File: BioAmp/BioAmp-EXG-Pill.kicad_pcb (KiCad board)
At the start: 4 copper layers, 39.2 x 11 mm, 44 parts, among them IC1 MCP3221A4T-E_OT, IC3 MAX1169BEUD+, J2 Conn_01x04_Pin, J3 Conn_01x04_Pin, J4 522710469, U1 TL074HIPWR

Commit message: Did component placement
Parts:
- removed IC1: MCP3221A4T-E_OT, ADC:SOT95P280X145-5N
- removed the R11 at (121.6, 98.2)
- C10, C11, C9: footprint Capacitor_SMD:C_0603_1608Metric_Pad1.08x0.95mm_HandSolder -> Capacitor_SMD:C_0402_1005Metric
- C4, D1, D2, D3, D4, D5, D6, JP4, JP5, JP6, R12, R13, R14, R17, R18, R19, R6: moved to B.Cu
- J4: footprint fpc_con:CON_522710469_MOL -> FPC_Connector:CON_522710469_MOL
- moved D1 77.9 mm to (115.8, 90.0)
- moved D2 77.7 mm to (115.8, 93.7)
- moved D3 75.5 mm to (118.0, 97.4)
- moved JP6 61.8 mm to (129.3, 91.2), turned to 90 degrees
- moved JP5 58.8 mm to (131.7, 91.2), turned to 90 degrees
- moved D4 58.2 mm to (136.6, 88.8)
- moved D6 57.6 mm to (137.1, 92.9), turned to 90 degrees
- moved R17 57.6 mm to (128.9, 93.5), turned to 180 degrees
- moved R14 57.3 mm to (114.6, 92.6), turned to 180 degrees
- moved R13 57.1 mm to (114.6, 91.2), turned to 180 degrees
- moved D5 56.9 mm to (137.1, 95.2), turned to -90 degrees
- moved JP4 55.9 mm to (134.2, 91.2), turned to 90 degrees
- moved R11 55.4 mm to (115.4, 98.7)
- moved R18 54.1 mm to (132.2, 93.5)
- moved R12 53.2 mm to (117.9, 92.6), turned to 180 degrees
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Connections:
- net Net-(R5-Pad1) renamed /U1A_out
- net Net-(U1B--) renamed /U1B_in
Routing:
- net VCC: track 52.1 -> 24.5 mm, vias 4 -> 2
- net bpfIN: track 26.7 -> 0.00 mm, vias 2 -> 0
- net /IN+_Prot: track 23.4 -> 0.00 mm
- net /IN-_Prot: track 21.8 -> 0.00 mm
- net bpfOUT: track 20.6 -> 0.00 mm, vias 2 -> 0
- net ampRef: track 12.7 -> 0.00 mm
- net /U1B_in: track 10.6 -> 0.00 mm, vias 2 -> 0
- net DRL: track 10.1 -> 0.00 mm
- net Net-(U1D-+): track 7.98 -> 0.00 mm
- net Net-(U1A--): track 7.16 -> 0.00 mm
- net inaOUT: track 8.46 -> 2.13 mm
- net SCL: track 12.1 -> 7.45 mm, vias 0 -> 1
- net /U1A_out: track 3.68 -> 0.00 mm
- net Net-(C1-Pad2): track 1.88 -> 0.00 mm
- net GND: track 1.51 -> 0.00 mm, vias 3 -> 1
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- added copper zone on In1.Cu, net GND
- added copper zone on In2.Cu, net GND
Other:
- board size 39.2 x 11 mm -> 43.2 x 13.1 mm

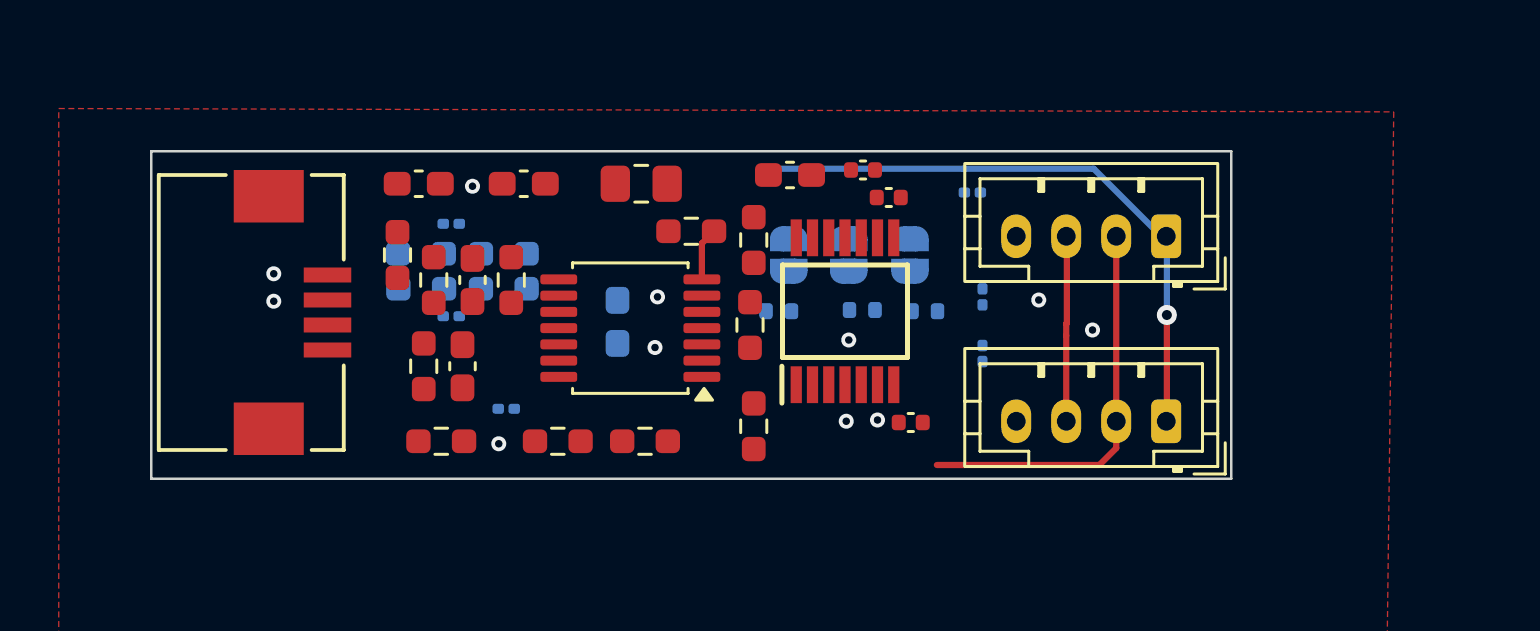
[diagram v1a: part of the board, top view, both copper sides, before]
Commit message: Added rounded edge with mounting hole
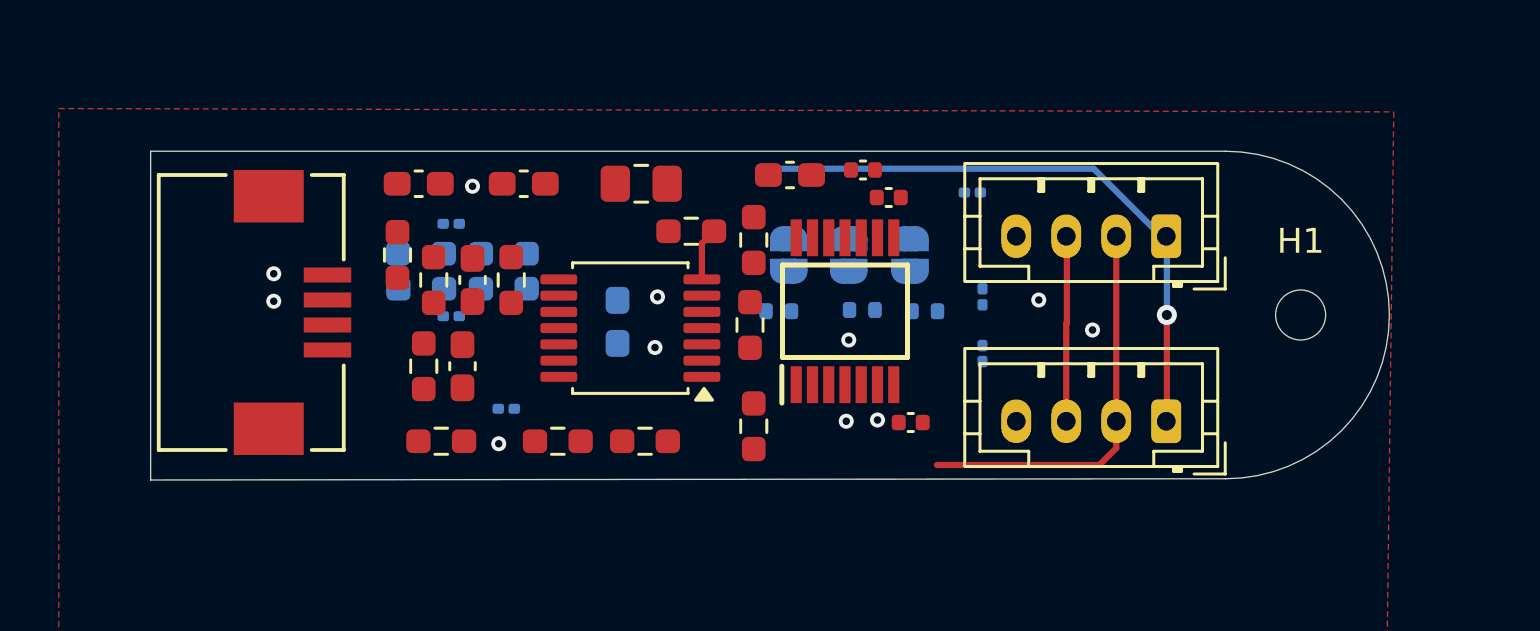
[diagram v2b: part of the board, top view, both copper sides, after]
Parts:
- added H1: MountingHole_Pad, MountingHole:MountingHole_2mm, F.Cu at (149.8, 93.7)
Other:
- board size 43.2 x 13.1 mm -> 49.5 x 13.2 mm
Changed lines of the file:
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@@
 		)
 		(embedded_fonts no)
+		(model "${CON_522710469_MOL}/2026-09-26_13-00-23.kicad_sym"
+			(offset
+				(xyz 0 0 0)
+			)
+			(scale
+				(xyz 1 1 1)
+			)
+			(rotate
+				(xyz 0 0 0)
+			)
+		)
 	)
 	(footprint "Capacitor_SMD:C_0805_2012Metric_Pad1.18x1.45mm_HandSolder"
@@
 		)
 	)
+	(footprint "MountingHole:MountingHole_2mm"
+		(layer "F.Cu")
+		(at 149.775 93.65)
+		(descr "Mounting Hole 2mm, no annular, generated by kicad-footprint-generator mountinghole.py")
+		(tags "mountinghole")
+		(property "Reference" "H1"
+			(at 0 -2.95 0)
+			(layer "F.SilkS")
+			(effects
+				(font
+					(size 1 1)
+					(thickness 0.15)
+				)
+			)
+		)
+		(property "Value" "MountingHole_Pad"
+			(at 0 2.95 0)
+			(layer "F.Fab")
+			(effects
+				(font
+					(size 1 1)
+					(thickness 0.15)
+				)
+			)
+		)
+		(property "Datasheet" ""
+			(at 0 0 0)
+			(layer "F.Fab")
+			(hide yes)
+			(effects
+				(font
+					(size 1.27 1.27)
+				)
+			)
+		)
+		(property "Description" "Mounting Hole with connection"
+			(at 0 0 0)
+			(layer "F.Fab")
+			(hide yes)
+			(effects
+				(font
+					(size 1.27 1.27)
+				)
+			)
+		)
+		(property "KiLib_Generator" "mounting_hardware/mounting_hole"
+			(at 0 0 0)
+			(layer "F.SilkS")
+			(hide yes)
+			(effects
+				(font
+					(size 1 1)
+					(thickness 0.15)
+				)
+			)
+		)
+		(property ki_fp_filters "MountingHole*Pad*")
+		(sheetname "/")
+		(sheetfile "BioAmp-EXG-Pill.kicad_sch")
+		(units
+			(unit
+				(name "A")
+				(pins "1")
+			)
+		)
+		(attr exclude_from_bom)
+		(duplicate_pad_numbers_are_jumpers no)
+		(fp_circle
+			(center 0 0)
+			(end 2 0)
+			(stroke
+				(width 0.15)
+				(type solid)
+			)
+			(fill no)
+			(layer "Cmts.User")
+		)
+		(fp_circle
+			(center 0 0)
+			(end 2.25 0)
+			(stroke
+				(width 0.05)
+				(type solid)
+			)
+			(fill no)
+			(layer "F.CrtYd")
+		)
+		(fp_text user "${REFERENCE}"
+			(at 0 0 0)
+			(layer "F.Fab")
+			(effects
+				(font
+					(size 1 1)
+					(thickness 0.15)
+				)
+			)
+		)
+		(pad "" np_thru_hole circle
+			(at 0 0)
+			(size 2 2)
+			(drill 2)
+			(layers "*.Cu" "*.Mask")
+		)
+		(embedded_fonts no)
+	)
 	(footprint "Resistor_SMD:R_0603_1608Metric_Pad0.98x0.95mm_HandSolder"
 		(layer "F.Cu")
@@
 	)
 	(gr_line
-		(start 148.3 100.15)
-		(end 147.3 100.15)
+		(start 153.4 93.65)
+		(end 153.375 109.475)
 		(stroke
 			(width 0.1)
@@
 	)
 	(gr_line
-		(start 148.9 87.05)
-		(end 147.25 87.05)
+		(start 103.775 87.1)
+		(end 103.775 100.25)
 		(stroke
-			(width 0.1)
+			(width 0.05)
 			(type default)
 		)
-		(layer "Dwgs.User")
+		(layer "Edge.Cuts")
 	)
-	(gr_rect
-		(start 103.8 87.1)
-		(end 147 100.2)
+	(gr_line
+		(start 103.775 100.25)
+		(end 146.775 100.2)
 		(stroke
-			(width 0.1)
-			(type solid)
+			(width 0.05)
+			(type default)
+		)
+		(layer "Edge.Cuts")
+	)
+	(gr_line
+		(start 146.775 87.1)
+		(end 103.775 87.1)
+		(stroke
+			(width 0.05)
+			(type default)
+		)
+		(layer "Edge.Cuts")
+	)
+	(gr_arc
+		(start 146.775 87.1)
+		(mid 153.325 93.65)
+		(end 146.775 100.2)
+		(stroke
+			(width 0.05)
+			(type default)
 		)
-		(fill no)
 		(layer "Edge.Cuts")
 	)
@@
 		(layer "Dwgs.User")
 		(pts
-			(xy 103.85 107.75) (xy 147 100.6)
+			(xy 103.85 107.75) (xy 153.35 107.75)
 		)
 		(height 0)
@@
 			(keep_text_aligned yes)
 		)
-		(gr_text "43.1500 mm"
-			(at 125.425 106.6 0)
+		(gr_text "49.5000 mm"
+			(at 128.6 106.6 0)
 			(layer "Dwgs.User")
 			(effects
@@
 		(layer "Dwgs.User")
 		(pts
-			(xy 148.9 87.05) (xy 149.3 100.15)
+			(xy 161.675 87.05) (xy 162.075 100.15)
 		)
 		(height 0)
@@
 		)
 		(gr_text "13.1000 mm"
-			(at 147.75 93.6 90)
+			(at 160.525 93.6 90)
 			(layer "Dwgs.User")
 			(effects
@@
 		)
 	)
+	(dimension
+		(type orthogonal)
+		(layer "Edge.Cuts")
+		(pts
+			(xy 146.775 93.65) (xy 153.325 93.65)
+		)
+		(height 0)
+		(orientation 0)
+		(format
+			(prefix "")
+			(suffix "")
+			(units 3)
+			(units_format 1)
+			(precision 4)
+		)
+		(style
+			(thickness 0.05)
+			(arrow_length 1.27)
+			(text_position_mode 0)
+			(arrow_direction outward)
+			(extension_height 0.58642)
+			(extension_offset 0.5)
+			(keep_text_aligned yes)
+		)
+		(gr_text "6.5500 mm"
+			(at 150.05 92.5 0)
+			(layer "Edge.Cuts")
+			(effects
+				(font
+					(size 1 1)
+					(thickness 0.15)
+				)
+			)
+		)
+	)
 	(segment
 		(start 144.425 97.9)
@@
 	)
 	(via
-		(at 141.45 94.25)
+		(at 108.7 92)
 		(size 0.6)
 		(drill 0.3)
 		(layers "F.Cu" "B.Cu")
 		(free yes)
-		(net "GND")
+		(net "IN-")
+	)
+	(via
+		(at 108.7 93.1)
+		(size 0.6)
+		(drill 0.3)
+		(layers "F.Cu" "B.Cu")
+		(free yes)
+		(net "IN+")
 	)
 	(segment
@@
 		(net "SDA")
 	)
-	(via
-		(at 108.7 92)
-		(size 0.6)
-		(drill 0.3)
-		(layers "F.Cu" "B.Cu")
-		(free yes)
-		(net "IN-")
-	)
-	(via
-		(at 108.7 93.1)
-		(size 0.6)
-		(drill 0.3)
-		(layers "F.Cu" "B.Cu")
-		(free yes)
-		(net "IN+")
-	)
-	(via
-		(at 124.05 92.925)
-		(size 0.6)
-		(drill 0.3)
-		(layers "F.Cu" "B.Cu")
-		(free yes)
-		(net "/IN+_Prot")
-	)
-	(via
-		(at 123.95 94.95)
-		(size 0.6)
-		(drill 0.3)
-		(layers "F.Cu" "B.Cu")
-		(free yes)
-		(net "/IN-_Prot")
-	)
 	(segment
 		(start 140.4 94.475)
@@
 		(net "SCL")
 	)
+	(via
+		(at 141.45 94.25)
+		(size 0.6)
+		(drill 0.3)
+		(layers "F.Cu" "B.Cu")
+		(free yes)
+		(net "GND")
+	)
+	(via
+		(at 123.95 94.95)
+		(size 0.6)
+		(drill 0.3)
+		(layers "F.Cu" "B.Cu")
+		(free yes)
+		(net "/IN-_Prot")
+	)
+	(via
+		(at 124.05 92.925)
+		(size 0.6)
+		(drill 0.3)
+		(layers "F.Cu" "B.Cu")
+		(free yes)
+		(net "/IN+_Prot")
+	)
 	(segment

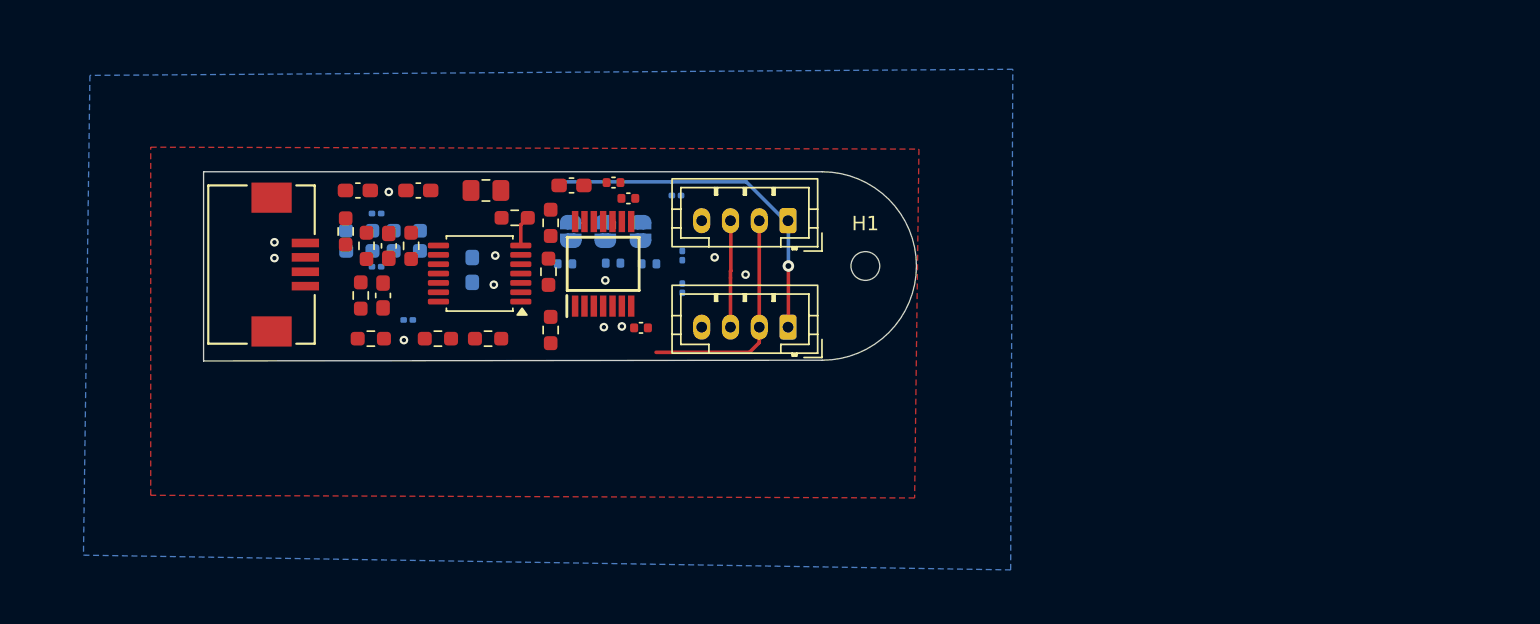
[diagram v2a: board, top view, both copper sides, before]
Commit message: Changed I2C connectors, added mounting holes and roundes edge
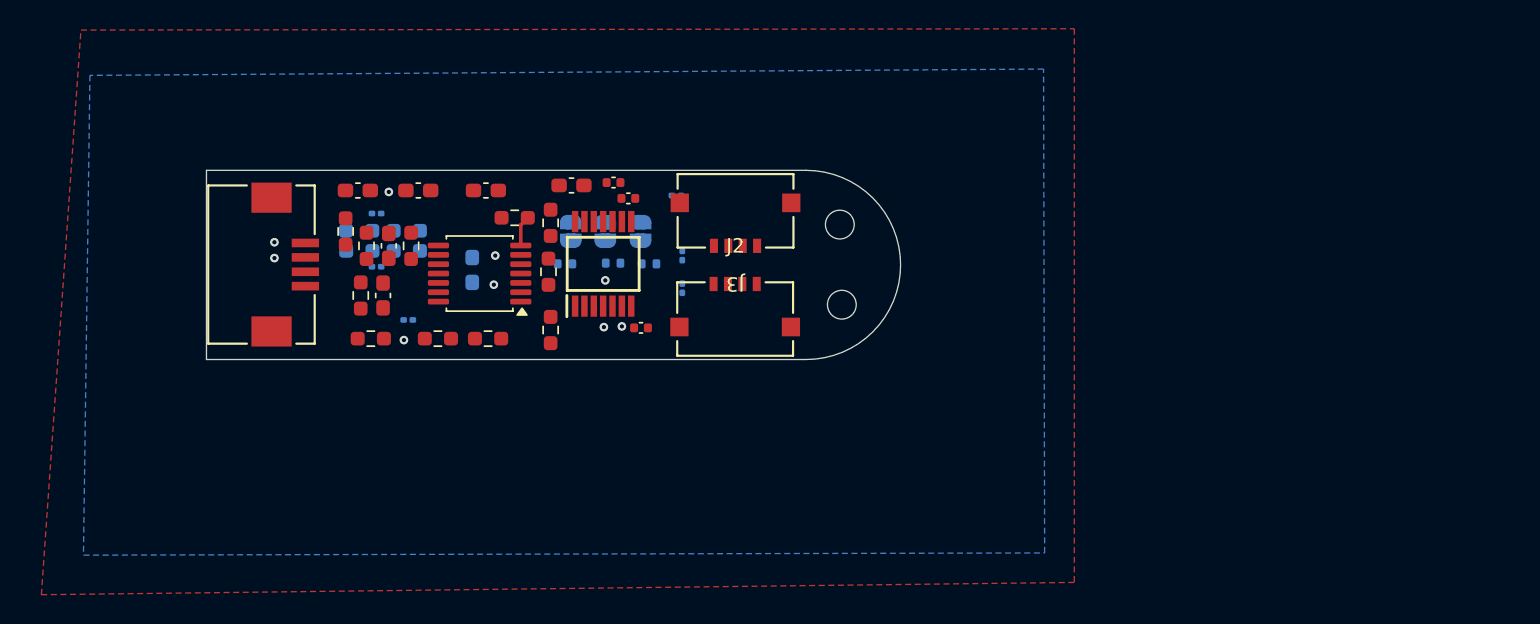
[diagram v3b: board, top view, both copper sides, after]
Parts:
- removed the H1 at (149.8, 93.7)
- added H1: MountingHole_Pad, MountingHole:MountingHole_2mm, F.Cu at (148.1, 96.3)
- added H1: MountingHole_Pad, MountingHole:MountingHole_2mm, F.Cu at (148.0, 90.8)
- C1: footprint Capacitor_SMD:C_0805_2012Metric_Pad1.18x1.45mm_HandSolder -> Capacitor_SMD:C_0603_1608Metric_Pad1.08x0.95mm_HandSolder
- J2, J3: footprint Connector_JST:JST_PH_B4B-PH-K_1x04_P2.00mm_Vertical -> I2C_Connector:CONN_5037630000-SD_04_MOL
- moved J2 8.87 mm to (140.8, 89.8), turned to 0 degrees
- moved J3 7.76 mm to (140.7, 97.3)
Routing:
- net VCC: track 24.5 -> 0.00 mm, vias 2 -> 1
- net SDA: track 15.9 -> 0.00 mm
- net SCL: track 7.45 -> 0.00 mm, vias 1 -> 0
- net GND: vias 1 -> 0
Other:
- board size 49.5 x 13.2 mm -> 48.2 x 13.2 mm

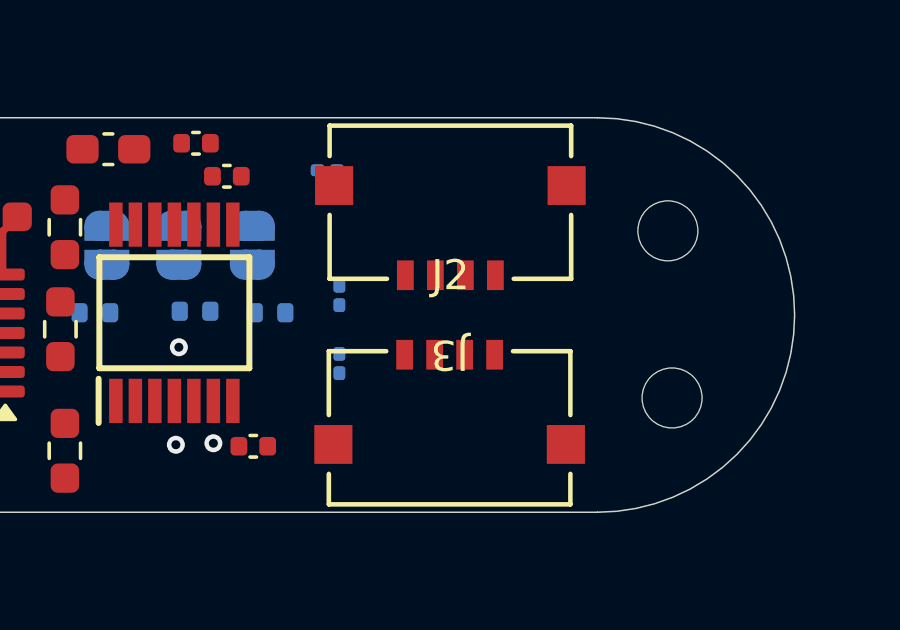
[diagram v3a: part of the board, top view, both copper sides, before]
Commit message: Save BioAmp layout before splitting analog and digital grounds
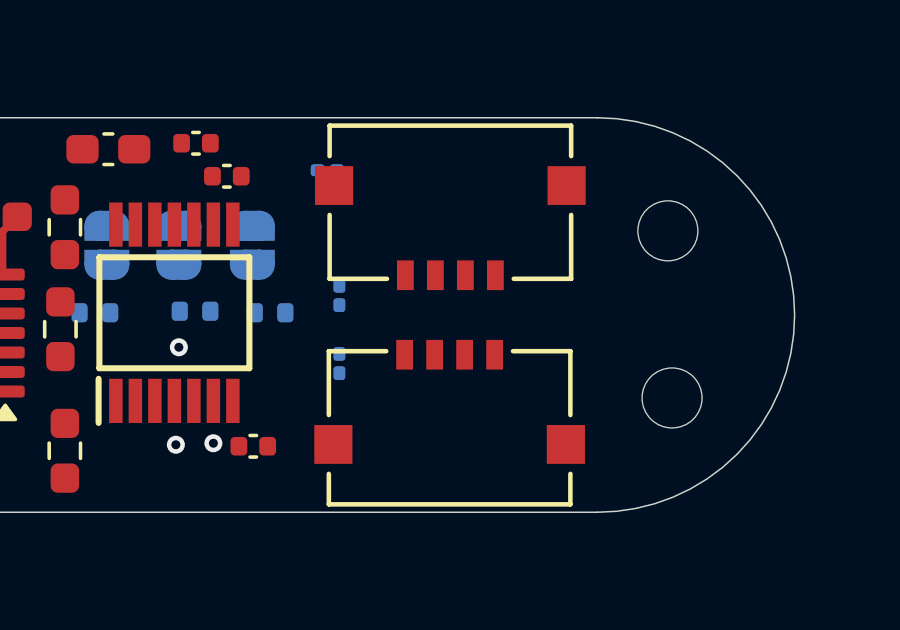
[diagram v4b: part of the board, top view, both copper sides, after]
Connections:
- J3 pad 1: VCC -> GND
- J3 pad 2: SDA -> SCL
- J3 pad 3: SCL -> SDA
- J3 pad 4: GND -> VCC
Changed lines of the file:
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@@
 			(unlocked yes)
 			(layer "F.SilkS")
+			(hide yes)
 			(effects
 				(font
@@
 		(sheetname "/")
 		(sheetfile "BioAmp-EXG-Pill.kicad_sch")
+		(units
+			(unit
+				(name "A")
+				(pins "1" "2" "3" "4")
+			)
+		)
 		(attr smd)
 		(duplicate_pad_numbers_are_jumpers no)
@@
 			(size 0.5588 0.9906)
 			(layers "F.Cu" "F.Mask" "F.Paste")
-			(net "VCC")
+			(net "GND")
 			(pinfunction "Pin_1_1")
 			(pintype "passive")
@@
 			(size 0.5588 0.9906)
 			(layers "F.Cu" "F.Mask" "F.Paste")
-			(net "SDA")
+			(net "SCL")
 			(pinfunction "Pin_2_2")
 			(pintype "passive")
@@
 			(size 0.5588 0.9906)
 			(layers "F.Cu" "F.Mask" "F.Paste")
-			(net "SCL")
+			(net "SDA")
 			(pinfunction "Pin_3_3")
 			(pintype "passive")
@@
 			(size 0.5588 0.9906)
 			(layers "F.Cu" "F.Mask" "F.Paste")
-			(net "GND")
+			(net "VCC")
 			(pinfunction "Pin_4_4")
 			(pintype "passive")
@@
 			(unlocked yes)
 			(layer "F.SilkS")
+			(hide yes)
 			(effects
 				(font
@@
 		(sheetname "/")
 		(sheetfile "BioAmp-EXG-Pill.kicad_sch")
+		(units
+			(unit
+				(name "A")
+				(pins "1" "2" "3" "4")
+			)
+		)
 		(attr smd)
 		(duplicate_pad_numbers_are_jumpers no)
